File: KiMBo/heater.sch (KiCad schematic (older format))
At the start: 55 parts

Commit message: Add more low-pass filters to the outputs, add reverse polarity protection
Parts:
- removed Q? (x3): DMP3098L-7, TO_SOT_Packages_SMD:SOT-23, symbol DMP3098L-7
- removed Q? (x5): 2N7002P,215, SOT-23, symbol 2N7002P,215
- added L? (x4): FBMH4532HM132-T, symbol INDUCTOR_Small
- added L? (x2): BLM31SN500SN1L, symbol INDUCTOR_Small
- added Q? (x3): DMP3098L-7, TO_SOT_Packages_SMD:SOT-23, symbol DMP3098L-7
- added Q? (x5): 2N7002, SOT-23, symbol 2N7002P,215
- Q?: value AOD417 -> IPD90P03P4-04
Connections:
- net +24V: now also Q?.2 (S), Q?.2 (S), Q?.2 (S)
- net BED_HEAT: now also L?.2, L?.2; no longer D?.1 (K), Q?.3 (D), R?.1
- net DOCK0_HEAT: now also L?.2; no longer D?.1 (K), R?.1
- net DOCK1_HEAT: now also L?.2; no longer D?.1 (K), R?.1
- net E_HEAT: now also L?.2; no longer D?.1 (K), Q?.3 (D), R?.1
- net GND: now also Q?.2 (S), Q?.2 (S), Q?.2 (S), Q?.2 (S), Q?.2 (S)
- net H_HEAT: now also L?.2; no longer D?.1 (K), R?.1
- net at R?.1: now also Q?.1 (G) (x5)
- net at R?.1, R?.2: now also Q?.1 (G) (x3)
- net at R?.2: now also Q?.3 (D) (x5)
- new net: D?.1 (K), L?.1, Q?.3 (D), R?.1 (x4)
- new net: D?.1 (K), L?.1, L?.1, Q?.3 (D), R?.1
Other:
- note added: "1/[2π√(LC)]≅1.56MHz\nT≅639.06ns"
- note added: "60mΩ max\nDC resistance\n1.3 kOhm @ 100MHz"
- note added: "Inductors in parallel\nin order to handle the current\n*half the impedance*"
- note added: "RC≅22.09μs"
- note added: "R_load(min)≅1.54Ω\nL_load≅0.8μH"
- note added: "~~2μH"
- note added: "~~7900pF input capacitance\nRC≅37.13μs"
- note removed: "AOD409"
- note removed: "check thermal characteristics\nsimulate RC output filter\nRC≅22.09μs"
- note removed: "only filtering the falling edge!"
- note removed: "~~920pF input capacitance\nRC≅4.324μs"
- moved on the sheet: C?, D?, Q?, R?

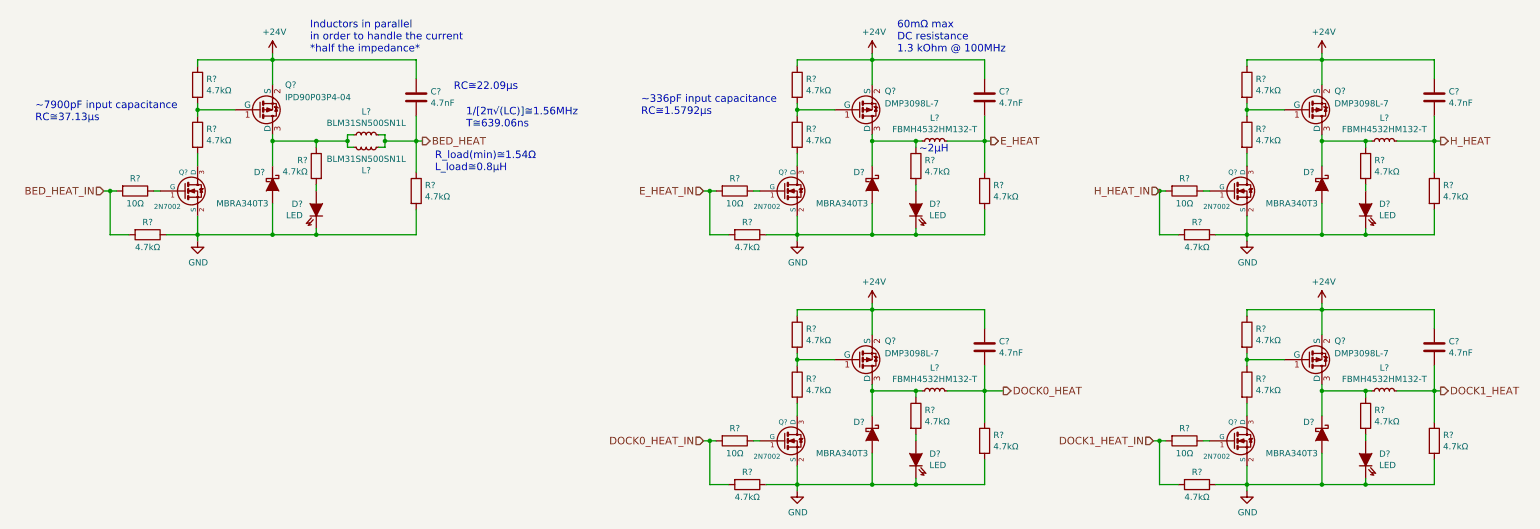
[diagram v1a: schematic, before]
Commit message: Update ferrite values, select fuse based on interrupt rating
The PSU needs to be able to supply at LEAST 25A to blow the fuse
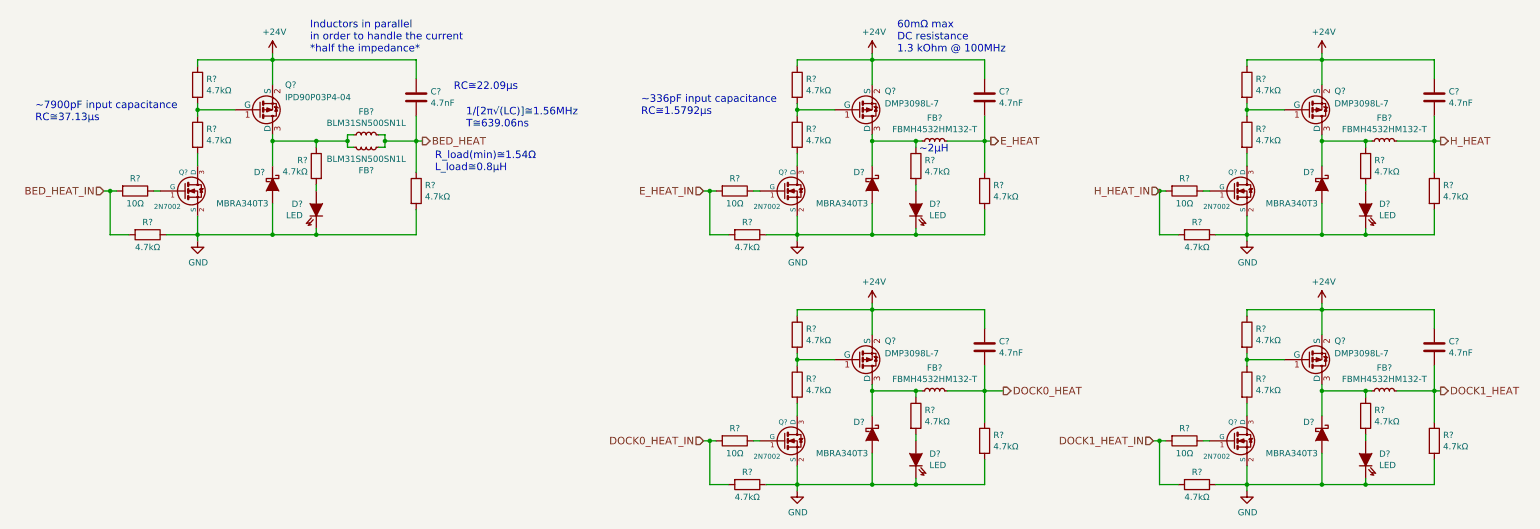
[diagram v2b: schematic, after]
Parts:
- gave numbers to parts that had none: 1
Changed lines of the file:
@@
 Connection ~ 4700 5050
 $Comp
-L INDUCTOR_Small L?
+L INDUCTOR_Small FB?
 U 1 1 5B59C6FB
 P 8850 5050
-F 0 "L?" V 9035 5050 50  0000 C CNN
+F 0 "FB?" V 9035 5050 50  0000 C CNN
 F 1 "FBMH4532HM132-T" V 8944 5050 50  0000 C CNN
 F 2 "" H 8850 5050 50  0000 C CNN
@@
 ~~2μH
 $Comp
-L INDUCTOR_Small L?
+L INDUCTOR_Small FB?
 U 1 1 5B5B3AB3
 P 4300 5000
-F 0 "L?" V 4485 5000 50  0000 C CNN
+F 0 "FB?" V 4485 5000 50  0000 C CNN
 F 1 "BLM31SN500SN1L" V 4394 5000 50  0000 C CNN
 F 2 "" H 4300 5000 50  0000 C CNN
@@
 $EndComp
 $Comp
-L INDUCTOR_Small L?
+L INDUCTOR_Small FB?
 U 1 1 5B5B3D92
 P 4300 5100
-F 0 "L?" V 4485 5100 50  0000 C CNN
+F 0 "FB?" V 4485 5100 50  0000 C CNN
 F 1 "BLM31SN500SN1L" V 4394 5100 50  0000 C CNN
 F 2 "" H 4300 5100 50  0000 C CNN
@@
 $EndComp
 $Comp
-L INDUCTOR_Small L?
+L INDUCTOR_Small FB?
 U 1 1 5B5DDDDE
 P 8850 7050
-F 0 "L?" V 9035 7050 50  0000 C CNN
+F 0 "FB?" V 9035 7050 50  0000 C CNN
 F 1 "FBMH4532HM132-T" V 8944 7050 50  0000 C CNN
 F 2 "" H 8850 7050 50  0000 C CNN
@@
 $EndComp
 $Comp
-L INDUCTOR_Small L?
+L INDUCTOR_Small FB?
 U 1 1 5B5DE039
 P 12450 7050
-F 0 "L?" V 12635 7050 50  0000 C CNN
+F 0 "FB?" V 12635 7050 50  0000 C CNN
 F 1 "FBMH4532HM132-T" V 12544 7050 50  0000 C CNN
 F 2 "" H 12450 7050 50  0000 C CNN
@@
 $EndComp
 $Comp
-L INDUCTOR_Small L?
+L INDUCTOR_Small FB?
 U 1 1 5B5DE359
 P 12450 5050
-F 0 "L?" V 12635 5050 50  0000 C CNN
+F 0 "FB?" V 12635 5050 50  0000 C CNN
 F 1 "FBMH4532HM132-T" V 12544 5050 50  0000 C CNN
 F 2 "" H 12450 5050 50  0000 C CNN

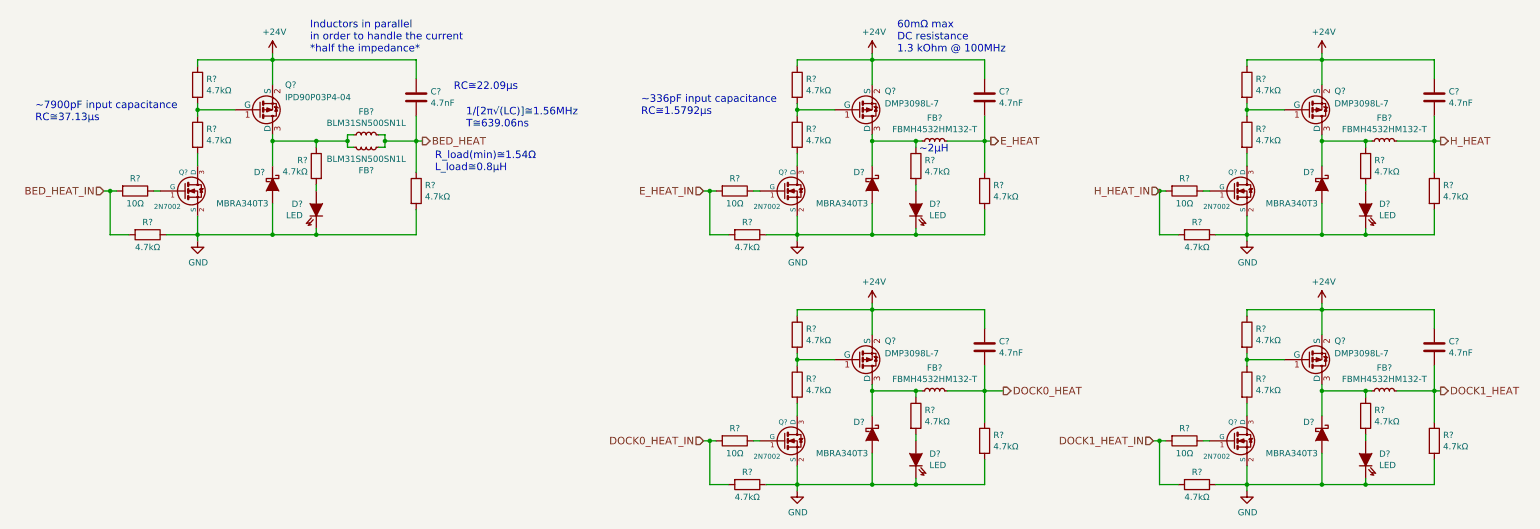
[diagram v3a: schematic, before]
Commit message: Annotate all components, now passing ERC, added ferrites to the rest of the connectors
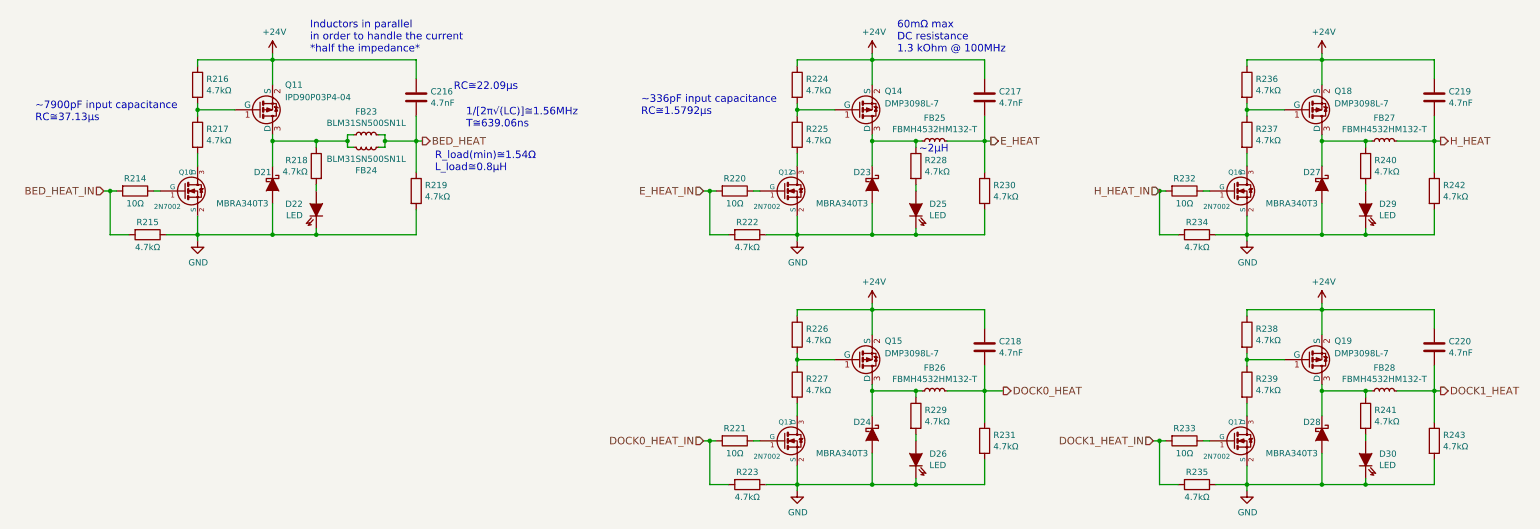
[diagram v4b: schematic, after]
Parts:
- gave numbers to parts that had none: 61

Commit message: Clean up various parts of the schematic, high level sheet has annoated modules
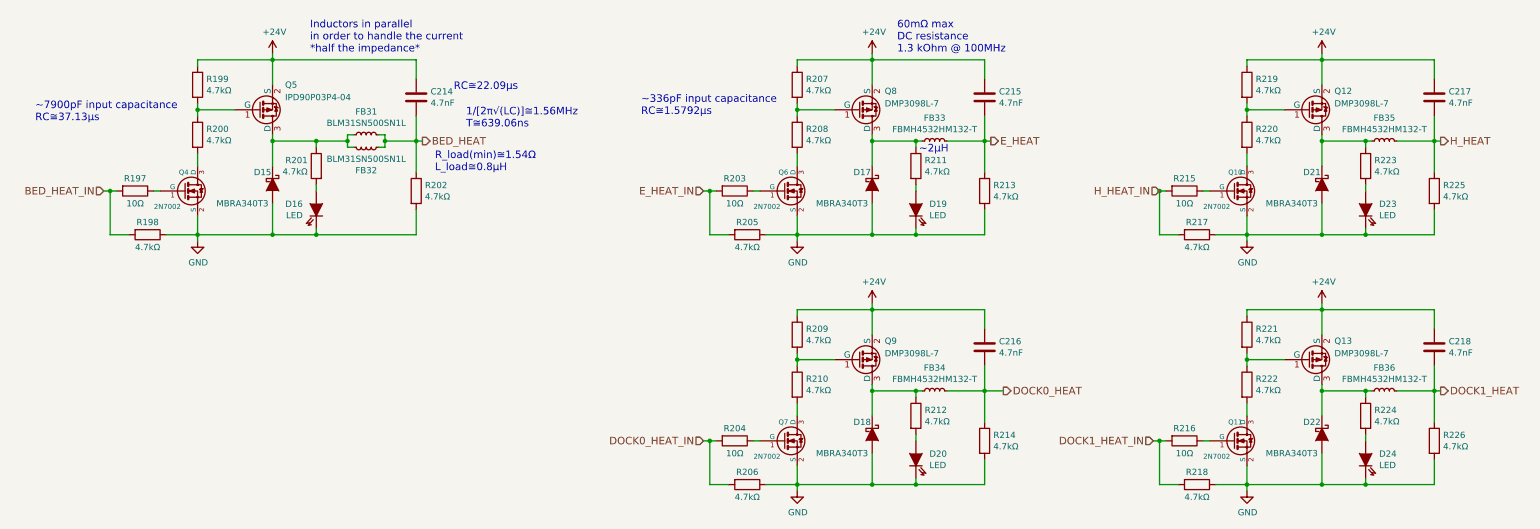
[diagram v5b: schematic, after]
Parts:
- renumbered C216 to C214, C217 to C215, C218 to C216, C219 to C217, C220 to C218, D21 to D15, D22 to D16, D23 to D17, D24 to D18, D25 to D19, D26 to D20, D27 to D21, D28 to D22, D29 to D23, D30 to D24, FB23 to FB31, FB24 to FB32, FB25 to FB33, FB26 to FB34, FB27 to FB35, FB28 to FB36, Q16 to Q10, Q17 to Q11, Q18 to Q12, Q19 to Q13, Q10 to Q4, Q11 to Q5, Q12 to Q6, Q13 to Q7, Q14 to Q8, Q15 to Q9, R214 to R197, R215 to R198, R216 to R199, R217 to R200, R218 to R201, R219 to R202, R220 to R203, R221 to R204, R222 to R205, R223 to R206, R224 to R207, R225 to R208, R226 to R209, R227 to R210, R228 to R211, R229 to R212, R230 to R213, R231 to R214, R232 to R215, R233 to R216, R234 to R217, R235 to R218, R236 to R219, R237 to R220, R238 to R221, R239 to R222, R240 to R223, R241 to R224, R242 to R225, R243 to R226

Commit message: Reorder the SS and EN lines from the shift registers such that the previously enabled/disabled motors stay enabled/disabled whilst writting to the shift register
Change 10k resistors to 4.7k, flip the open-drain inverter connected to B15 (PMTC_PGOOD)

Update the links in the README

Update the PDF schematic
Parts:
- Q10, Q11, Q4, Q6, Q7: footprint SOT-23 -> (none)
- Q12, Q13, Q8, Q9: footprint TO_SOT_Packages_SMD:SOT-23 -> (none)
- Q5: footprint TO_SOT_Packages_SMD:TO-252-2Lead -> (none)

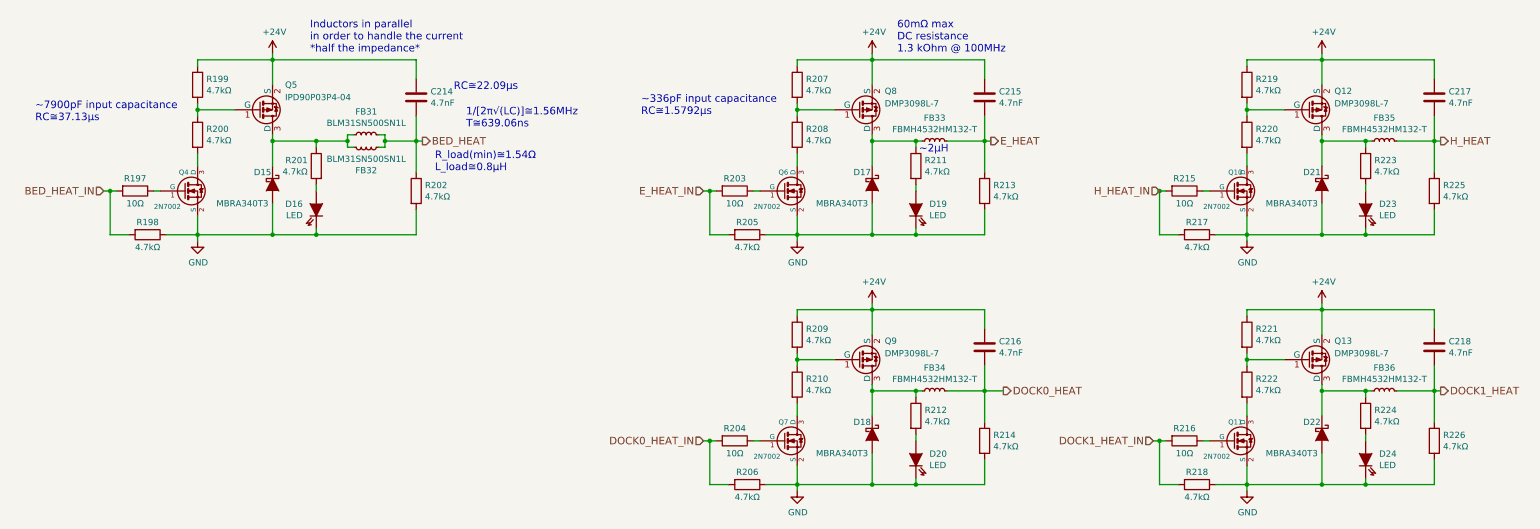
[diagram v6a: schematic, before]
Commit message: Entry of additional component values
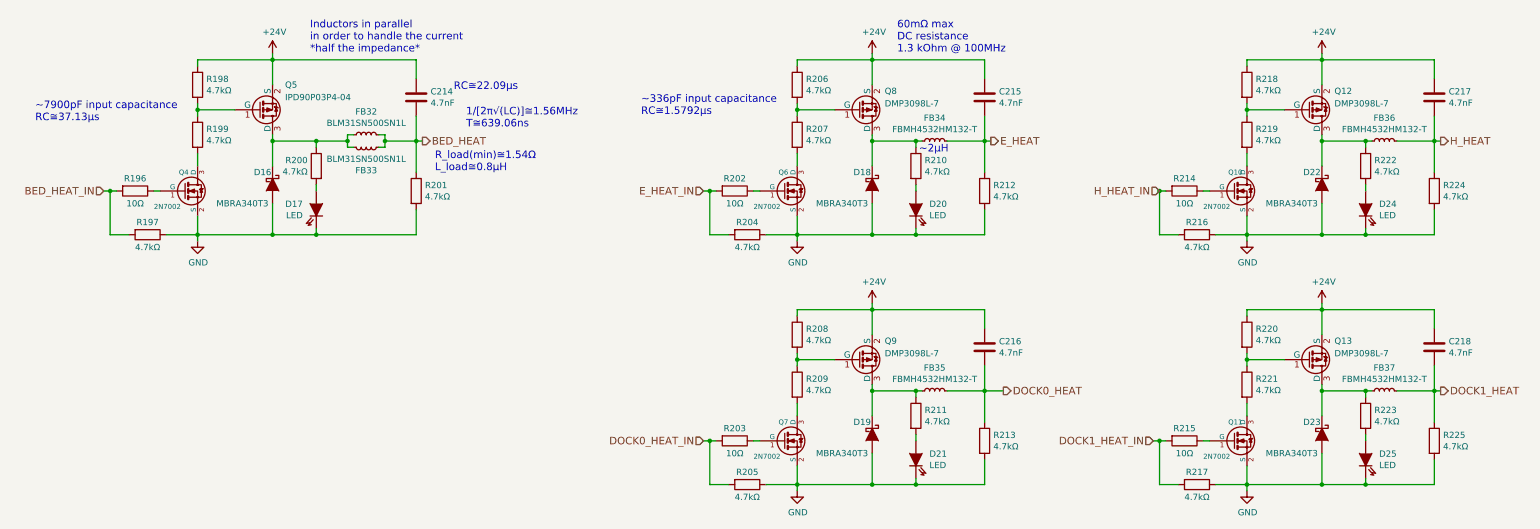
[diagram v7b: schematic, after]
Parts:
- renumbered D15 to D16, D16 to D17, D17 to D18, D18 to D19, D19 to D20, D20 to D21, D21 to D22, D22 to D23, D23 to D24, D24 to D25, FB31 to FB32, FB32 to FB33, FB33 to FB34, FB34 to FB35, FB35 to FB36, FB36 to FB37, R197 to R196, R198 to R197, R199 to R198, R200 to R199, R201 to R200, R202 to R201, R203 to R202, R204 to R203, R205 to R204, R206 to R205, R207 to R206, R208 to R207, R209 to R208, R210 to R209, R211 to R210, R212 to R211, R213 to R212, R214 to R213, R215 to R214, R216 to R215, R217 to R216, R218 to R217, R219 to R218, R220 to R219, R221 to R220, R222 to R221, R223 to R222, R224 to R223, R225 to R224, R226 to R225

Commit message: Add equivalent annotations document, associate more footprints
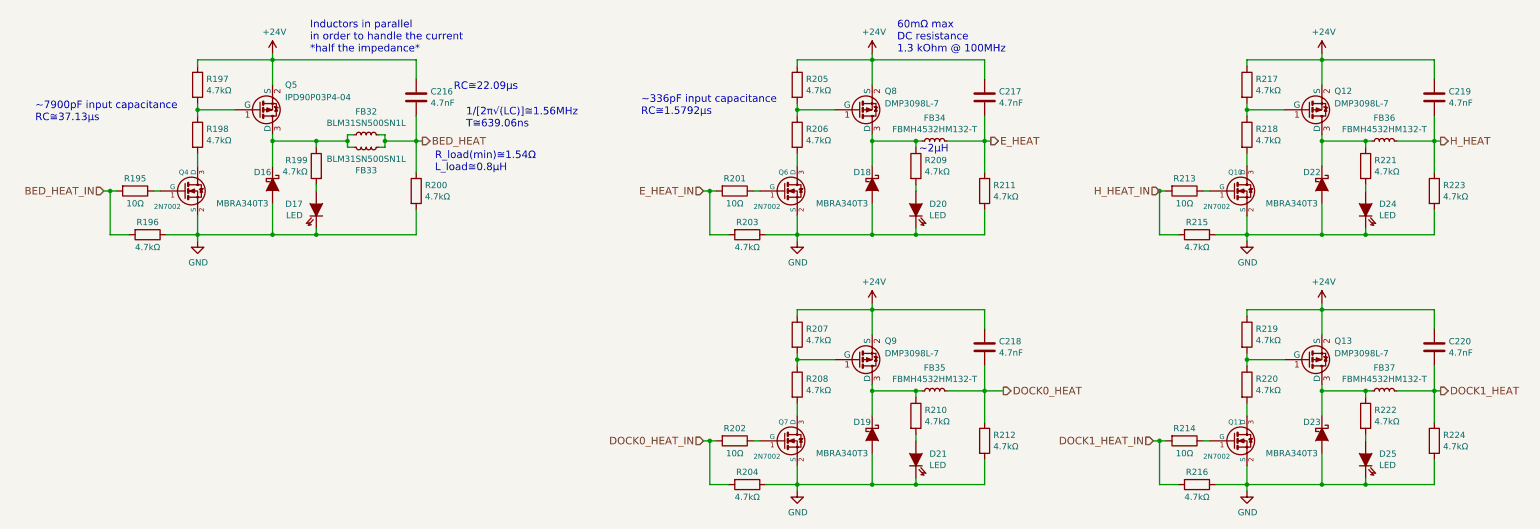
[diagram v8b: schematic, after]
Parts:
- C216: renamed from C214; footprint (none) -> Capacitors_SMD:C_0402
- C217: renamed from C215; footprint (none) -> Capacitors_SMD:C_0402
- C218: renamed from C216; footprint (none) -> Capacitors_SMD:C_0402
- C219: renamed from C217; footprint (none) -> Capacitors_SMD:C_0402
- C220: renamed from C218; footprint (none) -> Capacitors_SMD:C_0402
- renumbered R196 to R195, R197 to R196, R198 to R197, R199 to R198, R200 to R199, R201 to R200, R202 to R201, R203 to R202, R204 to R203, R205 to R204, R206 to R205, R207 to R206, R208 to R207, R209 to R208, R210 to R209, R211 to R210, R212 to R211, R213 to R212, R214 to R213, R215 to R214, R216 to R215, R217 to R216, R218 to R217, R219 to R218, R220 to R219, R221 to R220, R222 to R221, R223 to R222, R224 to R223, R225 to R224
